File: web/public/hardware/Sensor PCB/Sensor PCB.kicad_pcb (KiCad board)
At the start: 2 copper layers, 65 x 60 mm, 32 parts, among them J1 Conn_01x08_Pin, J2 Conn_01x08_Pin, J3 Conn_01x02_Pin, J4 Conn_01x02_Pin, U1 DRV5033AJxDBZ, U2 DRV5033AJxDBZ, U3 DRV5033AJxDBZ, U4 DRV5033AJxDBZ, U5 74LS11, U6 74LS11

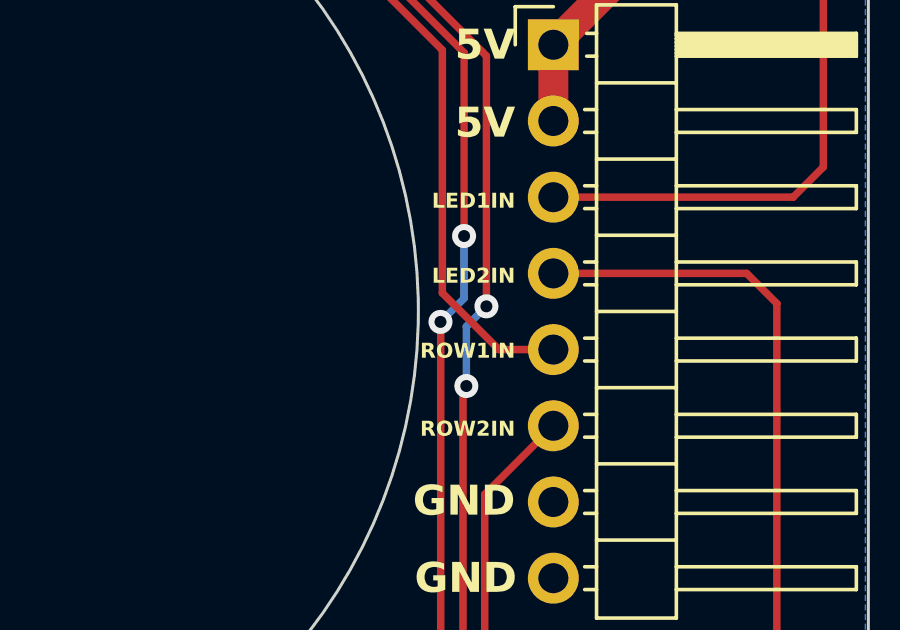
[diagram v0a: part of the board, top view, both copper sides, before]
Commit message: Fixed "out" signals' labelling on Sensor PCB
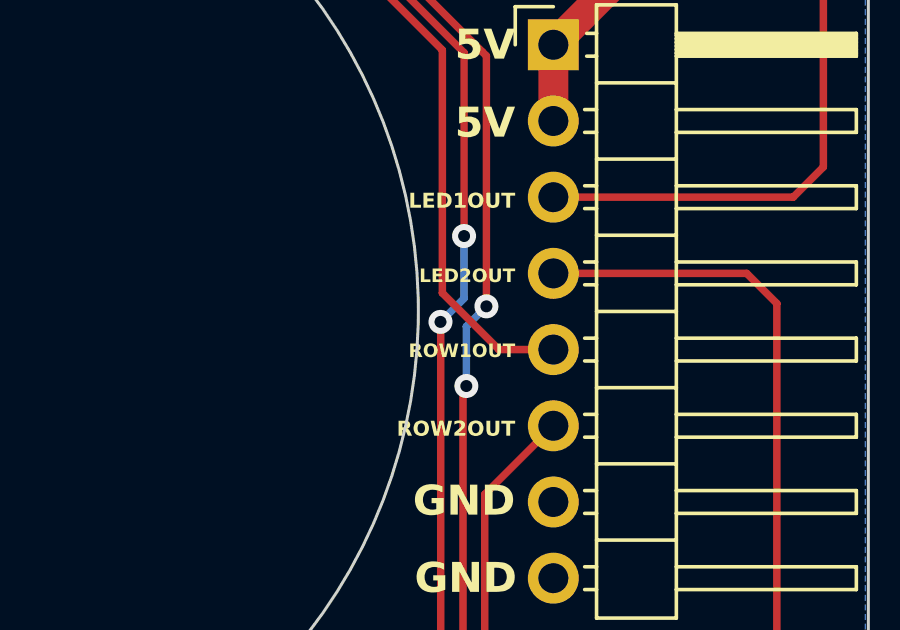
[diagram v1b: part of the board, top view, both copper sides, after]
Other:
- board text added: "LED1OUT"
- board text added: "LED2OUT"
- board text added: "ROW1OUT"
- board text added: "ROW2OUT"
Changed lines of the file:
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@@
     (effects (font (size 0.5 0.5) (thickness 0.1) bold) (justify left))
   )
-  (gr_text "ROW1IN" (at 163.23 91.325) (layer "F.SilkS")
-    (effects (font (size 0.5 0.5) (thickness 0.1) bold) (justify right))
+  (gr_text "ROW1OUT\n" (at 163.23 91.325) (layer "F.SilkS")
+    (effects (font (size 0.45 0.45) (thickness 0.1) bold) (justify right))
   )
   (gr_text "ROW1IN" (at 121.9 91.3) (layer "F.SilkS")
@@
     (effects (font (size 1 1) (thickness 0.2) bold) (justify right))
   )
-  (gr_text "ROW2IN\n" (at 163.23 93.925) (layer "F.SilkS")
+  (gr_text "ROW2OUT\n" (at 163.23 93.925) (layer "F.SilkS")
     (effects (font (size 0.5 0.5) (thickness 0.1) bold) (justify right))
   )
@@
     (effects (font (size 0.5 0.5) (thickness 0.1) bold) (justify left))
   )
-  (gr_text "LED1IN" (at 163.23 86.325) (layer "F.SilkS")
+  (gr_text "LED1OUT" (at 163.23 86.325) (layer "F.SilkS")
     (effects (font (size 0.5 0.5) (thickness 0.1) bold) (justify right))
   )
@@
     (effects (font (size 1 1) (thickness 0.2) bold) (justify right))
   )
-  (gr_text "LED2IN" (at 163.23 88.825) (layer "F.SilkS")
-    (effects (font (size 0.5 0.5) (thickness 0.1) bold) (justify right))
+  (gr_text "LED2OUT\n" (at 163.23 88.825) (layer "F.SilkS")
+    (effects (font (size 0.45 0.45) (thickness 0.1) bold) (justify right))
   )
   (gr_text "ROW1IN" (at 124.2 73.2 315) (layer "F.SilkS")

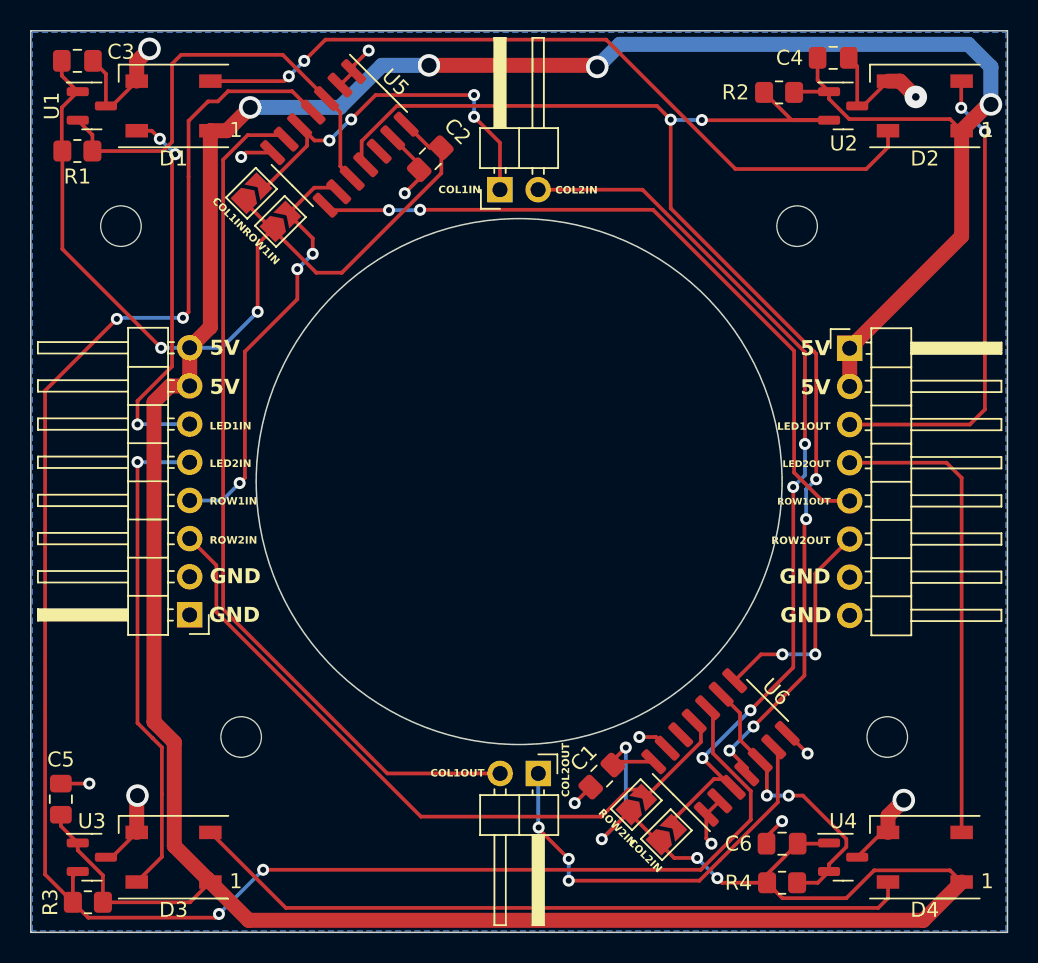
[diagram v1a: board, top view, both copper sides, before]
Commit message: Flip LED2 signal direction
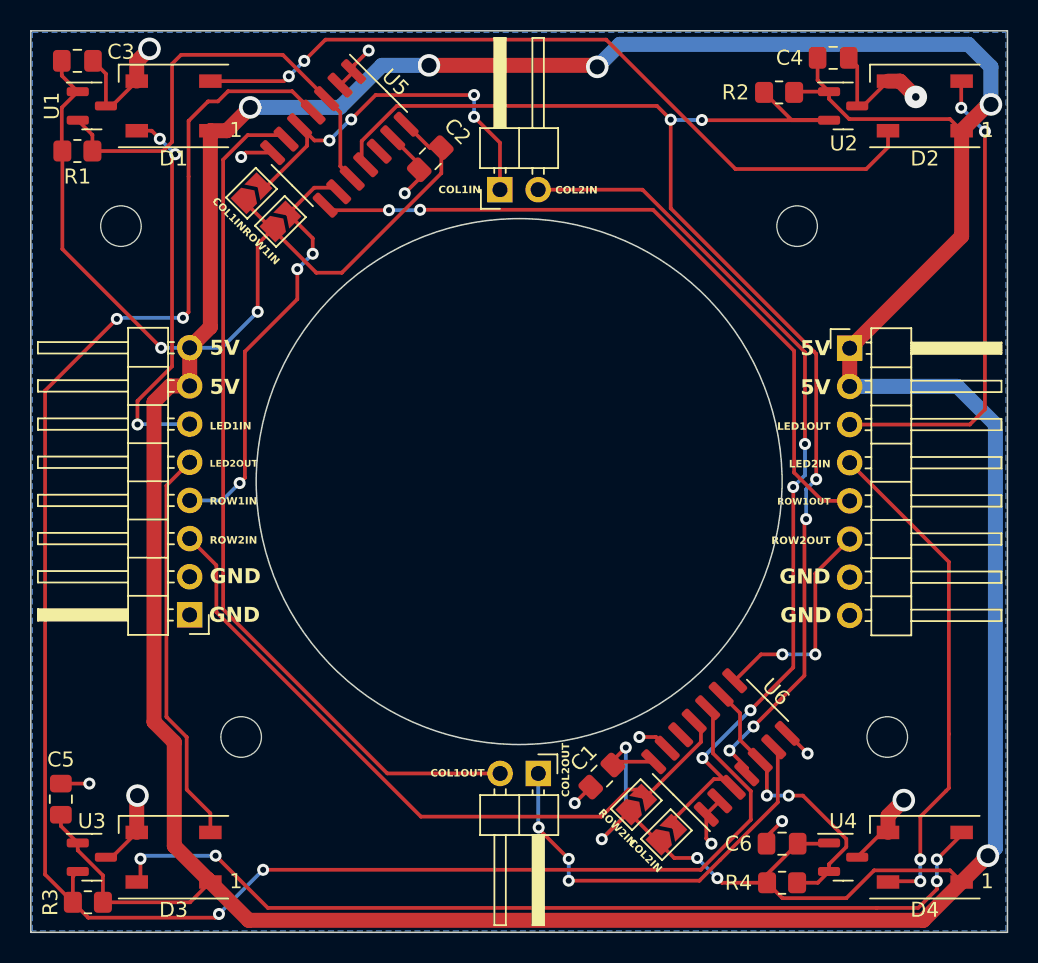
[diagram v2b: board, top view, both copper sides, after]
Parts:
- moved D3 50.0 mm to (119.5, 115.0)
- moved D4 50.0 mm to (169.5, 115.0)
- renumbered D4 to D3, D3 to D4
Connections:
- J1 pad 5: /LED2_IN -> /LED2_OUT
- J2 pad 4: /LED2_OUT -> /LED2_IN
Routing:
- net +5V: track 319.8 -> 361.9 mm, vias 10 -> 11
- net Net-(D3-DIN): track 48.5 -> 61.2 mm, vias 0 -> 4
- net /LED2_OUT: track 31.5 -> 26.5 mm
- net /LED2_IN: track 32.8 -> 33.5 mm, vias 1 -> 2
